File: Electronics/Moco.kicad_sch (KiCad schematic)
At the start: 37 parts, among them J1 Conn_01x04, J2 Conn_01x01, J3 Conn_ARM_JTAG_SWD_10, J4 Conn_01x03, J5 Conn_01x01, J6 Conn_01x04, J8 Conn_01x01, J9 Conn_01x01, U1 EFM32PG22C200FxxIM32, U2 SP485EN, U3 TMAG5273, U4 DRV8311, Y1 ECS-384-CDX-1983

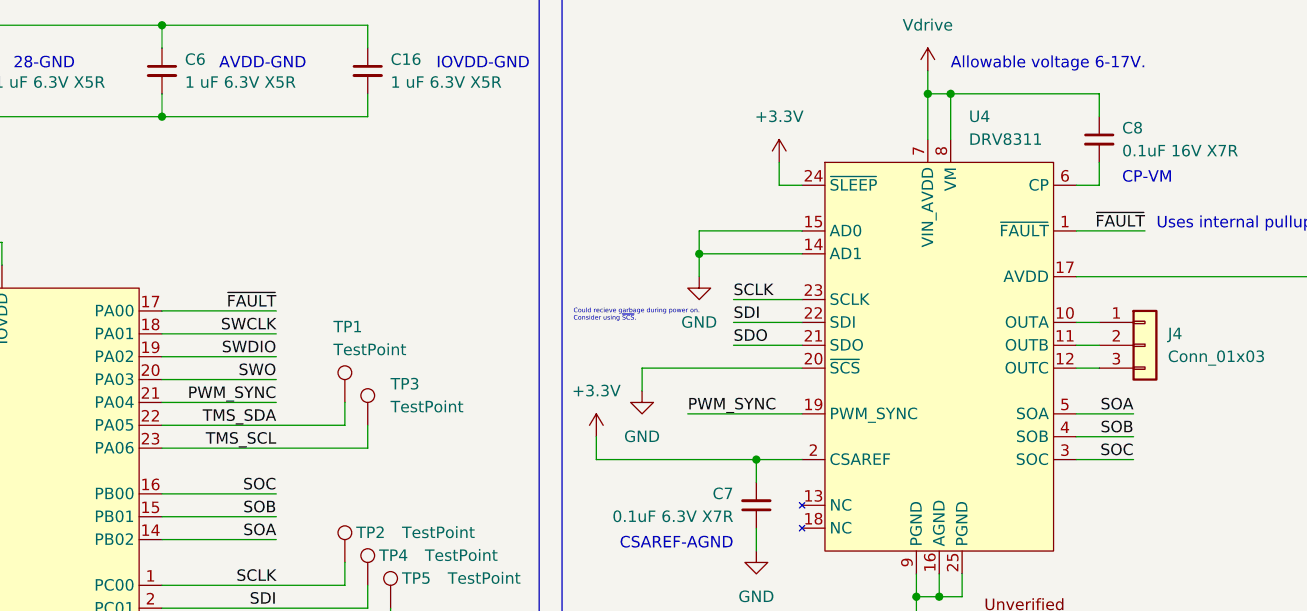
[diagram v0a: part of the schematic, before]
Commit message: Trade nFAULT for nSCS to avoid power on indeterminacy
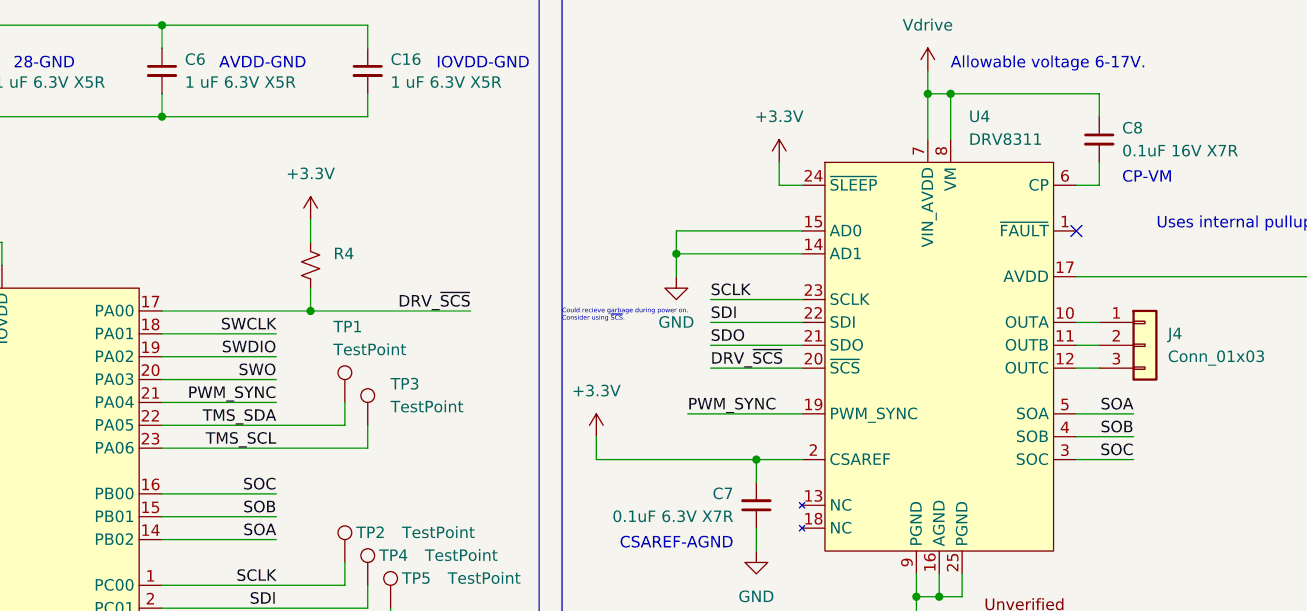
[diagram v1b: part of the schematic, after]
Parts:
- added R4: (no value), Resistor_SMD:R_0402_1005Metric, symbol Device:R_Small_US
- TP1, TP2, TP3, TP4, TP5: footprint TestPoint:TestPoint_Pad_1.5x1.5mm -> (none)
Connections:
- net +3V3: now also R4.1
- net GND: no longer U4.20 (~{SCS})
- net ~{FAULT}: no longer names the net of U4.1 (~{FAULT})
- net ~{FAULT}: no longer U1.17 (PA00)
- new net DRV_~{SCS}: R4.2, U1.17 (PA00), U4.20 (~{SCS})
- no-connect marks 2 -> 3

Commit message: Update silk (I think)
I am not entirely sure what changes are in this commit. I think it is mostly
just silk modifications.
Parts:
- R4: value (none) -> 10 kR
- TP1, TP2, TP3, TP4, TP5: footprint (none) -> TestPoint:TestPoint_Pad_1.0x1.0mm
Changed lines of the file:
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@@
       (effects (font (size 1.27 1.27)) (justify left))
     )
-    (property "Footprint" "" (id 2) (at 121.92 85.09 0)
+    (property "Footprint" "TestPoint:TestPoint_Pad_1.0x1.0mm" (id 2) (at 121.92 85.09 0)
       (effects (font (size 1.27 1.27)) hide)
     )
@@
       (effects (font (size 1.27 1.27)) (justify left))
     )
-    (property "Footprint" "" (id 2) (at 119.38 100.33 0)
+    (property "Footprint" "TestPoint:TestPoint_Pad_1.0x1.0mm" (id 2) (at 119.38 100.33 0)
       (effects (font (size 1.27 1.27)) hide)
     )
@@
       (effects (font (size 1.27 1.27)) (justify left))
     )
-    (property "Footprint" "" (id 2) (at 121.92 102.87 0)
+    (property "Footprint" "TestPoint:TestPoint_Pad_1.0x1.0mm" (id 2) (at 121.92 102.87 0)
       (effects (font (size 1.27 1.27)) hide)
     )
@@
       (effects (font (size 1.27 1.27)) (justify left))
     )
-    (property "Footprint" "" (id 2) (at 119.38 82.55 0)
+    (property "Footprint" "TestPoint:TestPoint_Pad_1.0x1.0mm" (id 2) (at 119.38 82.55 0)
       (effects (font (size 1.27 1.27)) hide)
     )
@@
       (effects (font (size 1.27 1.27)) (justify left))
     )
-    (property "Footprint" "" (id 2) (at 124.46 105.41 0)
+    (property "Footprint" "TestPoint:TestPoint_Pad_1.0x1.0mm" (id 2) (at 124.46 105.41 0)
       (effects (font (size 1.27 1.27)) hide)
     )
@@
       (effects (font (size 1.27 1.27)) (justify left))
     )
-    (property "Value" "" (id 1) (at 113.03 68.5799 0)
-      (effects (font (size 1.27 1.27)) (justify left))
-    )
+    (property "Value" "10 kR" (id 1) (at 113.03 68.5799 0)
+      (effects (font (size 1.27 1.27)) (justify left))
+    )

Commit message: Switch from EFM32PG22 to EFR32BG22
The EFM32PG22 is not currently available. The EFR32BG22 is downwards
pin-for-pin compatible with it so I'll use that instead (for now).
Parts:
- U1: value EFM32PG22C200FxxIM32 -> (none); symbol DStutman_MCU:EFM32PG22C200FxxIM32 -> Library:EFR32BG22C200FxxIM32
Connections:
- no-connect marks 3 -> 4
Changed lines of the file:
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@@
   (junction (at 163.83 140.97) (diameter 0) (color 0 0 0 0)
   )
+  (no_connect (at 53.34 123.19))
   (no_connect (at 53.34 85.09))
   (no_connect (at 344.17 130.81))
@@
     (pin "2")
   )
-  (symbol (lib_id "DStutman_MCU:EFM32PG22C200FxxIM32") (at 73.66 97.79 0) (unit 1)
+  (symbol (lib_id "Library:EFR32BG22C200FxxIM32") (at 73.66 97.79 0) (unit 1)
     (in_bom yes) (on_board yes) (fields_autoplaced)
     (property "Reference" "U1" (id 0) (at 75.6794 128.27 0)
       (effects (font (size 1.27 1.27)) (justify left))
     )
-    (property "Value" "EFM32PG22C200FxxIM32" (id 1) (at 75.6794 130.81 0)
-      (effects (font (size 1.27 1.27)) (justify left))
-    )
+    (property "Value" "" (id 1) (at 75.6794 130.81 0)
+      (effects (font (size 1.27 1.27)) (justify left))
+    )

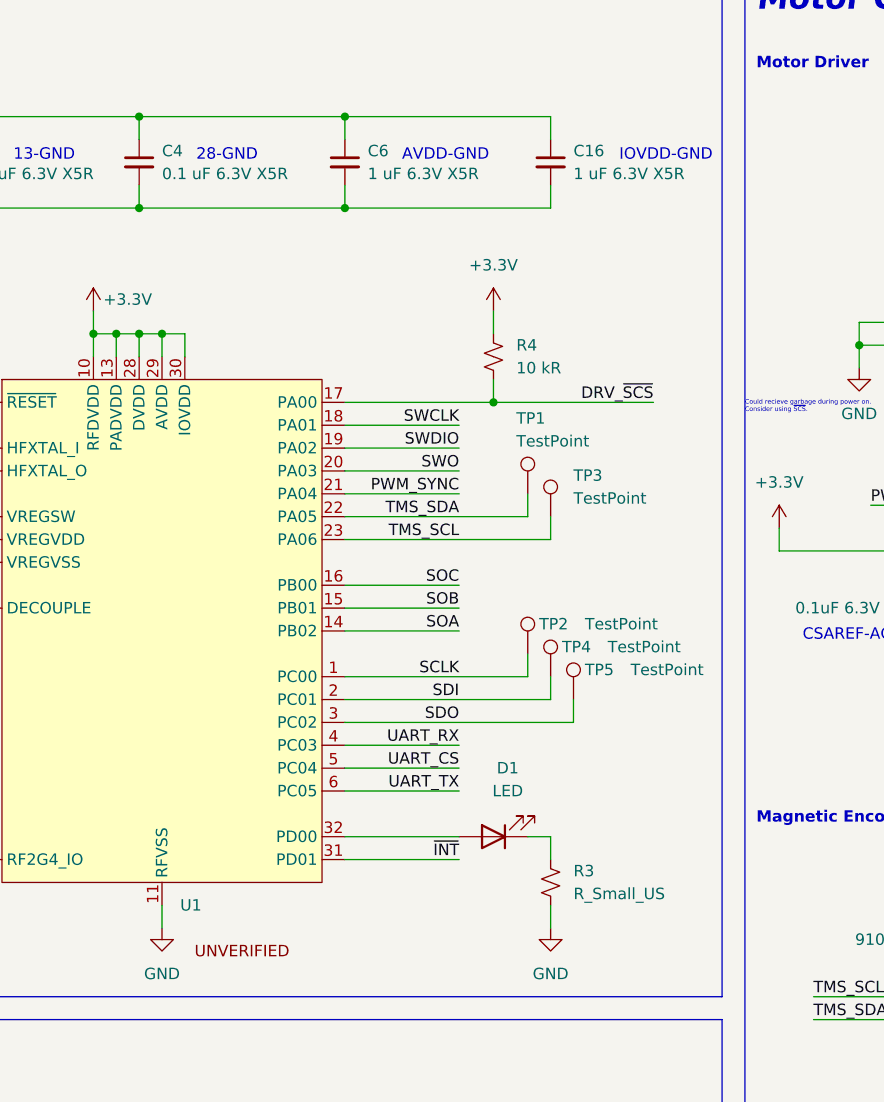
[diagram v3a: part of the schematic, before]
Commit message: Update EFR32 part number
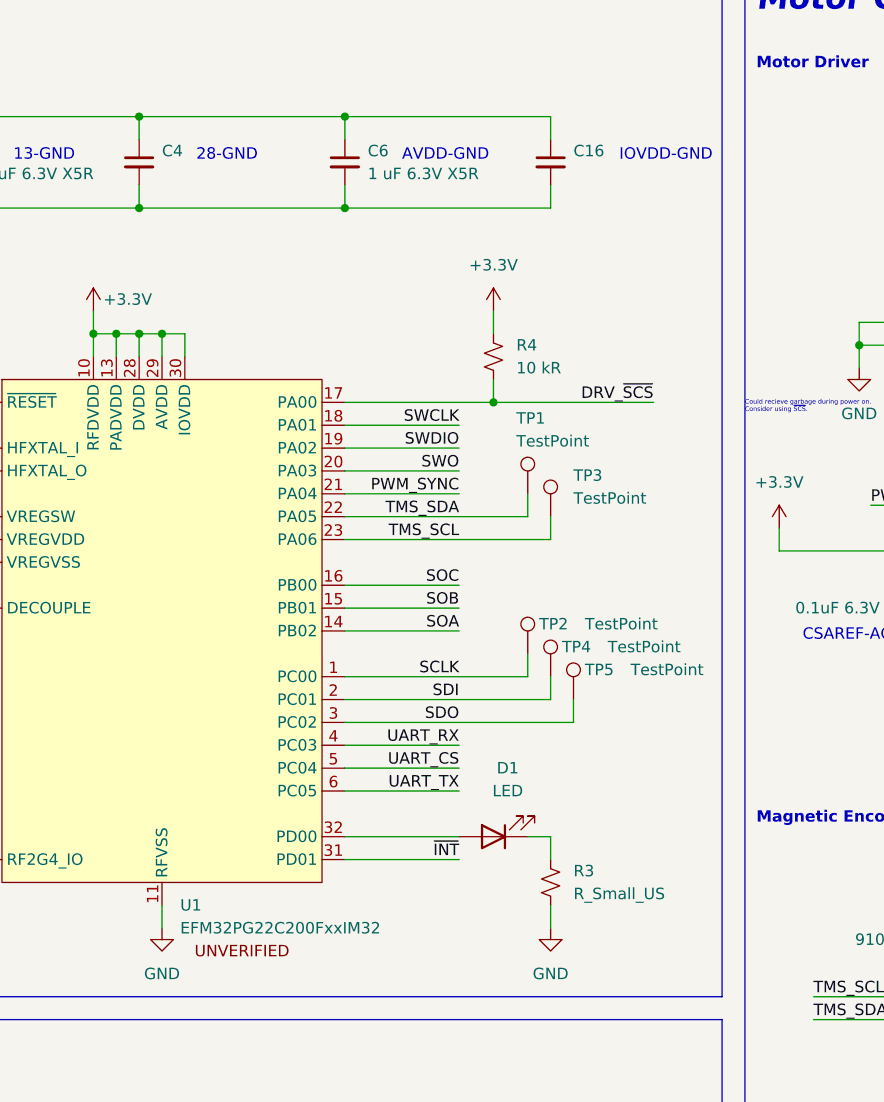
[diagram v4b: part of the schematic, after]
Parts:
- C16: value 1 uF 6.3V X5R -> (none)
- C4: value 0.1 uF 6.3V X5R -> (none)
- U1: value (none) -> EFM32PG22C200FxxIM32
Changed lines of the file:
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@@
       (effects (font (size 1.27 1.27)) (justify left))
     )
-    (property "Value" "0.1 uF 6.3V X5R" (id 1) (at 73.66 46.9962 0)
+    (property "Value" "" (id 1) (at 73.66 46.9962 0)
       (effects (font (size 1.27 1.27)) (justify left))
     )
@@
       (effects (font (size 1.27 1.27)) (justify left))
     )
-    (property "Value" "" (id 1) (at 75.6794 130.81 0)
+    (property "Value" "EFM32PG22C200FxxIM32" (id 1) (at 75.6794 130.81 0)
       (effects (font (size 1.27 1.27)) (justify left))
     )
@@
       (effects (font (size 1.27 1.27)) (justify left))
     )
-    (property "Value" "1 uF 6.3V X5R" (id 1) (at 119.38 46.9962 0)
+    (property "Value" "" (id 1) (at 119.38 46.9962 0)
       (effects (font (size 1.27 1.27)) (justify left))
     )
@@
     )
     (path "/38fb5cb4-62b0-453c-a0cd-70f0377918e1"
-      (reference "C4") (unit 1) (value "0.1 uF 6.3V X5R") (footprint "Capacitor_SMD:C_0402_1005Metric")
+      (reference "C4") (unit 1) (value "1 uF 6.3V X5R") (footprint "Capacitor_SMD:C_0402_1005Metric")
     )
     (path "/27da2ae3-72dc-4398-adbe-9877cfb05dfd"
@@
     )
     (path "/a4ca4859-4de5-4905-abe9-999d28b168e2"
-      (reference "C16") (unit 1) (value "1 uF 6.3V X5R") (footprint "Capacitor_SMD:C_0402_1005Metric")
+      (reference "C16") (unit 1) (value "0.1 uF 6.3V X5R") (footprint "Capacitor_SMD:C_0402_1005Metric")
     )
     (path "/68513806-7dc4-4ce3-a311-86049a308f19"

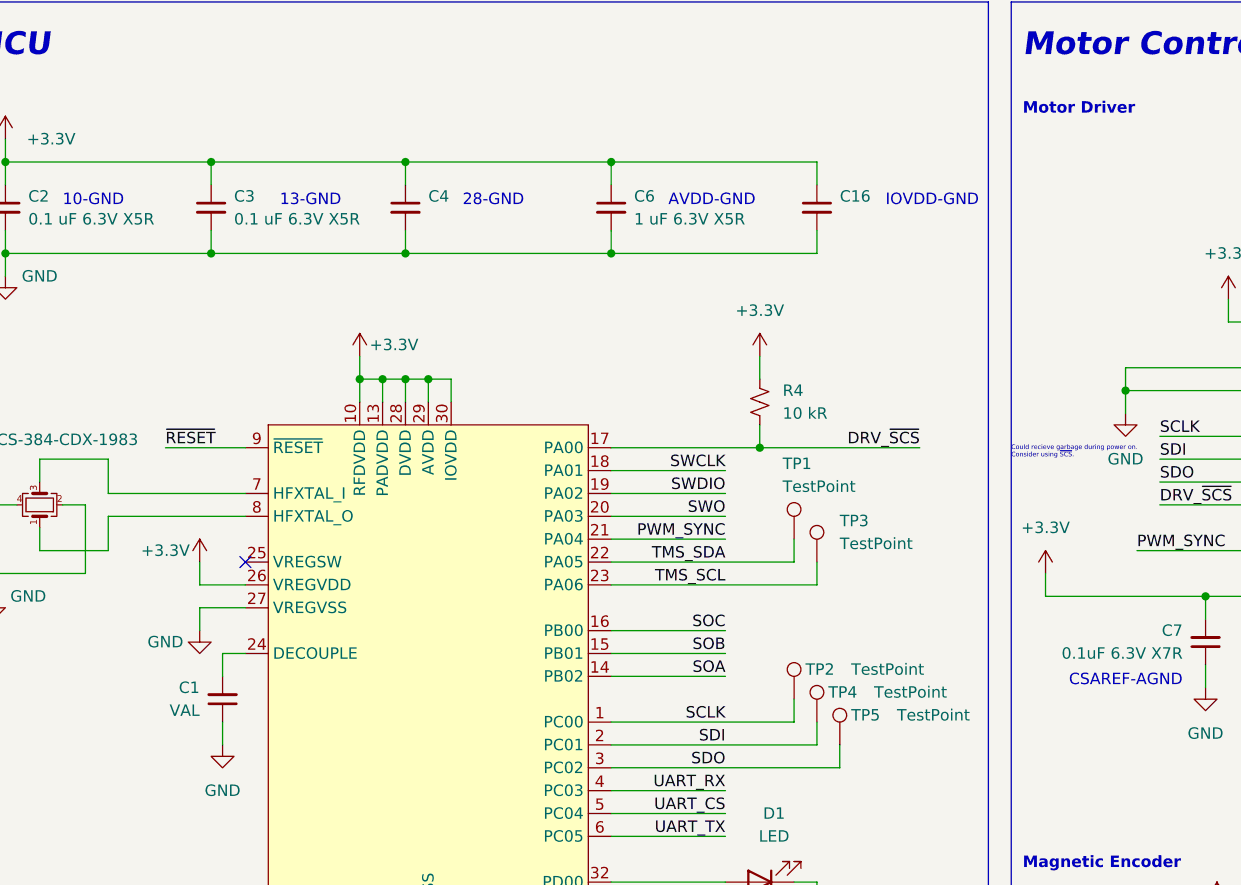
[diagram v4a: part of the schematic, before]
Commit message: Improve decoupling
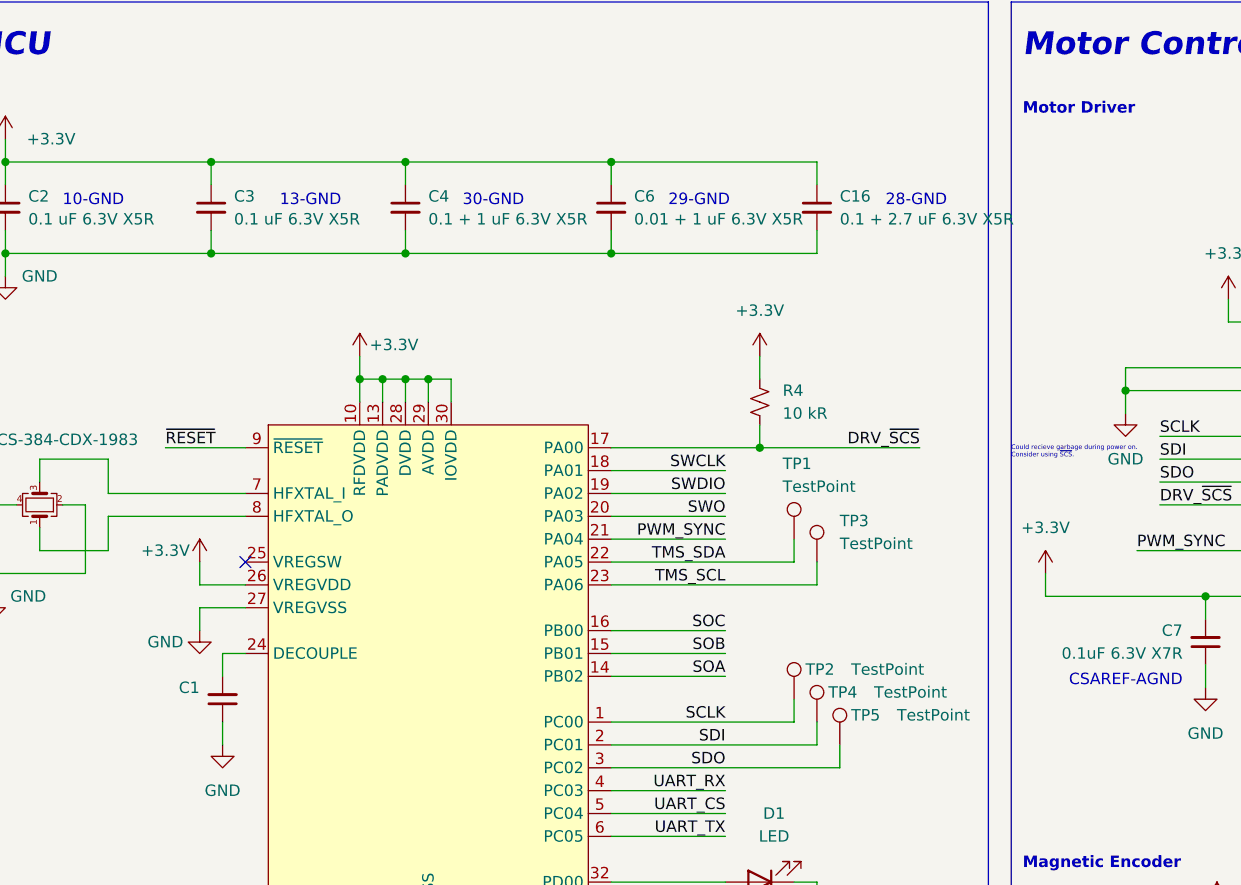
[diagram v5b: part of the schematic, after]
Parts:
- C1: value VAL -> (none)
- C16: value (none) -> 0.1 + 2.7 uF 6.3V X5R
- C4: value (none) -> 0.1 + 1 uF 6.3V X5R
- C6: value 1 uF 6.3V X5R -> 0.01 + 1 uF 6.3V X5R
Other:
- note added: "29-GND"
- note added: "30-GND"
- note removed: "AVDD-GND"
- note removed: "IOVDD-GND"
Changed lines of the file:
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@@
     (stroke (width 0) (type default) (color 0 0 0 0))
   )
-  (wire (pts (xy 93.98 40.64) (xy 71.12 40.64))
+  (wire (pts (xy 71.12 40.64) (xy 93.98 40.64))
     (stroke (width 0) (type default) (color 0 0 0 0))
   )
@@
     (stroke (width 0) (type default) (color 0 0 0 0))
   )
-  (wire (pts (xy 93.98 50.8) (xy 71.12 50.8))
+  (wire (pts (xy 71.12 50.8) (xy 93.98 50.8))
     (stroke (width 0) (type default) (color 0 0 0 0))
   )
@@
     (effects (font (size 2.54 2.54) (thickness 0.254) bold italic) (justify left bottom))
   )
-  (text "IOVDD-GND" (at 124.46 45.72 0)
+  (text "28-GND" (at 124.46 45.72 0)
     (effects (font (size 1.27 1.27)) (justify left bottom))
   )
@@
     (effects (font (size 1.27 1.27)) (justify left bottom))
   )
-  (text "AVDD-GND" (at 100.33 45.72 0)
+  (text "29-GND" (at 100.33 45.72 0)
     (effects (font (size 1.27 1.27)) (justify left bottom))
   )
@@
     (effects (font (size 1.27 1.27)) (justify left bottom))
   )
-  (text "28-GND" (at 77.47 45.72 0)
+  (text "30-GND" (at 77.47 45.72 0)
     (effects (font (size 1.27 1.27)) (justify left bottom))
   )
@@
       (effects (font (size 1.27 1.27)) (justify left))
     )
-    (property "Value" "1 uF 6.3V X5R" (id 1) (at 96.52 46.9962 0)
+    (property "Value" "0.01 + 1 uF 6.3V X5R" (id 1) (at 96.52 46.9962 0)
       (effects (font (size 1.27 1.27)) (justify left))
     )
@@
       (effects (font (size 1.27 1.27)) (justify right))
     )
-    (property "Value" "VAL" (id 1) (at 48.26 101.5935 0)
+    (property "Value" "" (id 1) (at 48.26 101.5935 0)
       (effects (font (size 1.27 1.27)) (justify right))
     )
@@
       (effects (font (size 1.27 1.27)) (justify left))
     )
-    (property "Value" "" (id 1) (at 73.66 46.9962 0)
+    (property "Value" "0.1 + 1 uF 6.3V X5R" (id 1) (at 73.66 46.9962 0)
       (effects (font (size 1.27 1.27)) (justify left))
     )
@@
       (effects (font (size 1.27 1.27)) (justify left))
     )
-    (property "Value" "" (id 1) (at 119.38 46.9962 0)
+    (property "Value" "0.1 + 2.7 uF 6.3V X5R" (id 1) (at 119.38 46.9962 0)
       (effects (font (size 1.27 1.27)) (justify left))
     )
@@
     )
     (path "/21d60392-f9d6-465b-8725-094da3bed2f0"
-      (reference "C1") (unit 1) (value "VAL") (footprint "Capacitor_SMD:C_0402_1005Metric")
+      (reference "C1") (unit 1) (value "1 uF 6.3V X5R") (footprint "Capacitor_SMD:C_0402_1005Metric")
     )
     (path "/bcfc37b1-e0fd-40f1-8325-351ffad26fda"
@@
     )
     (path "/38fb5cb4-62b0-453c-a0cd-70f0377918e1"
-      (reference "C4") (unit 1) (value "1 uF 6.3V X5R") (footprint "Capacitor_SMD:C_0402_1005Metric")
+      (reference "C4") (unit 1) (value "0.1 + 1 uF 6.3V X5R") (footprint "Capacitor_SMD:C_0402_1005Metric")
     )
     (path "/27da2ae3-72dc-4398-adbe-9877cfb05dfd"
@@
     )
     (path "/00f4f29f-9733-4015-857c-bd030c9fa78e"
-      (reference "C6") (unit 1) (value "1 uF 6.3V X5R") (footprint "Capacitor_SMD:C_0402_1005Metric")
+      (reference "C6") (unit 1) (value "0.01 + 1 uF 6.3V X5R") (footprint "Capacitor_SMD:C_0402_1005Metric")
     )
     (path "/be590212-ba3d-45af-ba87-1d3ad615e5af"
@@
     )
     (path "/a4ca4859-4de5-4905-abe9-999d28b168e2"
-      (reference "C16") (unit 1) (value "0.1 uF 6.3V X5R") (footprint "Capacitor_SMD:C_0402_1005Metric")
+      (reference "C16") (unit 1) (value "0.1 + 2.7 uF 6.3V X5R") (footprint "Capacitor_SMD:C_0402_1005Metric")
     )
     (path "/68513806-7dc4-4ce3-a311-86049a308f19"
